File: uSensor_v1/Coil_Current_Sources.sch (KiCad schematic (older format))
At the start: 25 parts, among them Q3 BC847PN-7-F, Q4 BC847PN-7-F, U14 TBD

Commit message: Components checked.
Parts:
- U14: value TBD -> MCP6H02-E/SN; MFR TBD -> Mircochip; MPN TBD -> MCP6H02-E/SN
- U14: value TBD -> MCP6H02-E/SN; MFR TBD -> Microchip; MPN TBD -> MCP6H02-E/SN
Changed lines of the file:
@@
 P 5850 3700
 F 0 "U14" H 5850 4067 50  0000 C CNN
-F 1 "TBD" H 5850 3976 50  0000 C CNN
+F 1 "MCP6H02-E/SN" H 5850 3976 50  0000 C CNN
 F 2 "Sentisa-IC:SO-8" H 5850 3700 50  0001 C CNN
 F 3 "" H 5850 3700 50  0001 C CNN
-F 4 "TBD" H 5850 3700 50  0001 C CNN "MFR"
-F 5 "TBD" H 5850 3700 50  0001 C CNN "MPN"
+F 4 "Mircochip" H 5850 3700 50  0001 C CNN "MFR"
+F 5 "MCP6H02-E/SN" H 5850 3700 50  0001 C CNN "MPN"
 	1    5850 3700
 	1    0    0    -1
@@
 P 5850 7000
 F 0 "U14" H 5850 7367 50  0000 C CNN
-F 1 "TBD" H 5850 7276 50  0000 C CNN
+F 1 "MCP6H02-E/SN" H 5850 7276 50  0000 C CNN
 F 2 "Sentisa-IC:SO-8" H 5850 7000 50  0001 C CNN
 F 3 "" H 5850 7000 50  0001 C CNN
-F 4 "TBD" H 5850 7000 50  0001 C CNN "MFR"
-F 5 "TBD" H 5850 7000 50  0001 C CNN "MPN"
+F 4 "Microchip" H 5850 7000 50  0001 C CNN "MFR"
+F 5 "MCP6H02-E/SN" H 5850 7000 50  0001 C CNN "MPN"
 	2    5850 7000
 	1    0    0    -1

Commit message: Layout in progress (adding vias)
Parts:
- U14: value TBD -> MCP6H02-E/SN; MFR TBD -> Microchip; MPN TBD -> MCP6H02-E/SN
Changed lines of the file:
@@
 P 9550 4700
 F 0 "U14" H 9508 4746 50  0000 L CNN
-F 1 "TBD" H 9508 4655 50  0000 L CNN
+F 1 "MCP6H02-E/SN" H 9508 4655 50  0000 L CNN
 F 2 "Sentisa-IC:SO-8" H 9550 4700 50  0001 C CNN
 F 3 "" H 9550 4700 50  0001 C CNN
-F 4 "TBD" H 9550 4700 50  0001 C CNN "MFR"
-F 5 "TBD" H 9550 4700 50  0001 C CNN "MPN"
+F 4 "Microchip" H 9550 4700 50  0001 C CNN "MFR"
+F 5 "MCP6H02-E/SN" H 9550 4700 50  0001 C CNN "MPN"
 	3    9550 4700
 	1    0    0    -1

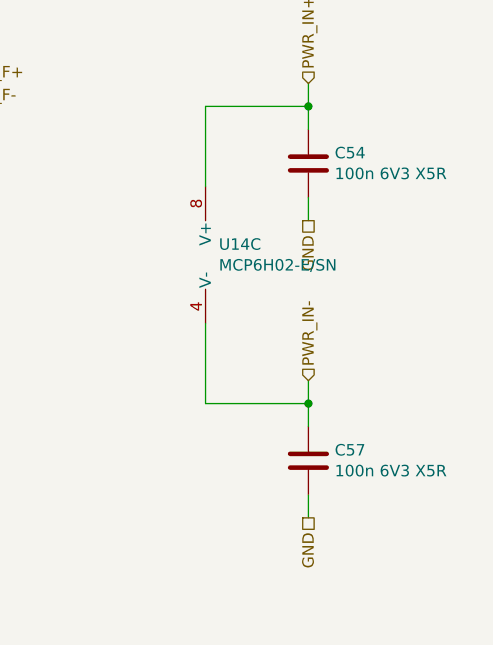
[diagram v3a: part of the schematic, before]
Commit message: Unificated some components. Order ready.
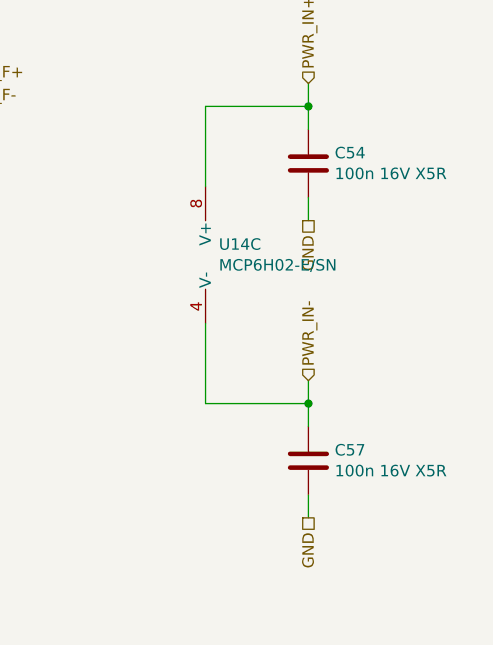
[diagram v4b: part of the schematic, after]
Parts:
- C54, C57: value 100n 6V3 X5R -> 100n 16V X5R
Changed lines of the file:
@@
 AR Path="/5C839FF6/5C4809A6" Ref="C56"  Part="1"
 F 0 "C54" H 10015 4346 50  0000 L CNN
-F 1 "100n 6V3 X5R" H 10015 4255 50  0000 L CNN
+F 1 "100n 16V X5R" H 10015 4255 50  0000 L CNN
 F 2 "Capacitor_SMD:C_0603_1608Metric_Pad1.05x0.95mm_HandSolder" H 9938 4150 50  0001 C CNN
 F 3 "~" H 9900 4300 50  0001 C CNN
@@
 AR Path="/5C839FF6/5CE2BE0E" Ref="C?"  Part="1"
 F 0 "C57" H 10015 5646 50  0000 L CNN
-F 1 "100n 6V3 X5R" H 10015 5555 50  0000 L CNN
+F 1 "100n 16V X5R" H 10015 5555 50  0000 L CNN
 F 2 "Capacitor_SMD:C_0603_1608Metric_Pad1.05x0.95mm_HandSolder" H 9938 5450 50  0001 C CNN
 F 3 "~" H 9900 5600 50  0001 C CNN
